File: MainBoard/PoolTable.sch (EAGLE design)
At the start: 77 parts, among them IC1 LM317MBSTT3, IC2 LM317MBSTT3, IC3 LM317MBSTT3, IC5 MIC2026-1YM, IC7 AP2331W-7, J1 USB_A_SMT_FEMALE, J2 USB_A_SMT_FEMALE, J4 SD_CARD_SOCKET, Q1 DMG1012T-7, Q2 DMG1012T-7, Q3 DMG1012T-7, U1 TMP102, U2 TMP102, U3 TMP102, U4 TMP102, U5 LAN9512-JZX, U6 FSUSB42UMX

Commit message: Syncing work
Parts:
- added SJ2, SJ3, SJ4, SJ5, SJ6, SJ7, SJ8, SJ9: (no value), jumper:SJ
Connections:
- removed net CPU1_CD1_SCL: CAM0.20, CAM1.20
- removed net CPU1_CD1_SDA: CAM0.21, CAM1.21
- new net CPU1_CAM0_IO0: SJ9.1
- new net CPU1_CAM0_IO1: SJ8.1
- new net CPU1_CAM0_SCL: SJ7.1
- new net CPU1_CAM0_SDA: SJ6.1
- new net CPU1_CAM1_IO0: SJ5.1
- new net CPU1_CAM1_IO1: SJ4.1
- new net CPU1_CAM1_SCL: SJ3.1
- new net CPU1_CAM1_SDA: SJ2.1
- net CPU1_CAM0_C_N: now also CPU1.144/CAM0_CN*
- net CPU1_CAM0_C_P: now also CPU1.142/CAM0_CP*
- net CPU1_CAM0_D0_N: now also CPU1.138/CAM0_DN0*
- net CPU1_CAM0_D0_P: now also CPU1.136/CAM0_DP0*
- net CPU1_CAM0_D1_N: now also CPU1.150/CAM0_DN1*
- net CPU1_CAM0_D1_P: now also CPU1.148/CAM0_DP1*
- net CPU1_GPIO28: now also SJ6.2
- net CPU1_GPIO29: now also SJ7.2
- net CPU1_GPIO30: now also SJ8.2
- net CPU1_GPIO31: now also SJ9.2
- net CPU1_SCL0: now also SJ3.2
- net CPU1_SCL1: now also SJ5.2
- net CPU1_SDA0: now also SJ2.2
- net CPU1_SDA1: now also SJ4.2
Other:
- note added: "I2C MAY BE CONFIGURED WRONG TO HAVE ACCESS TO BOTH BUSSES"

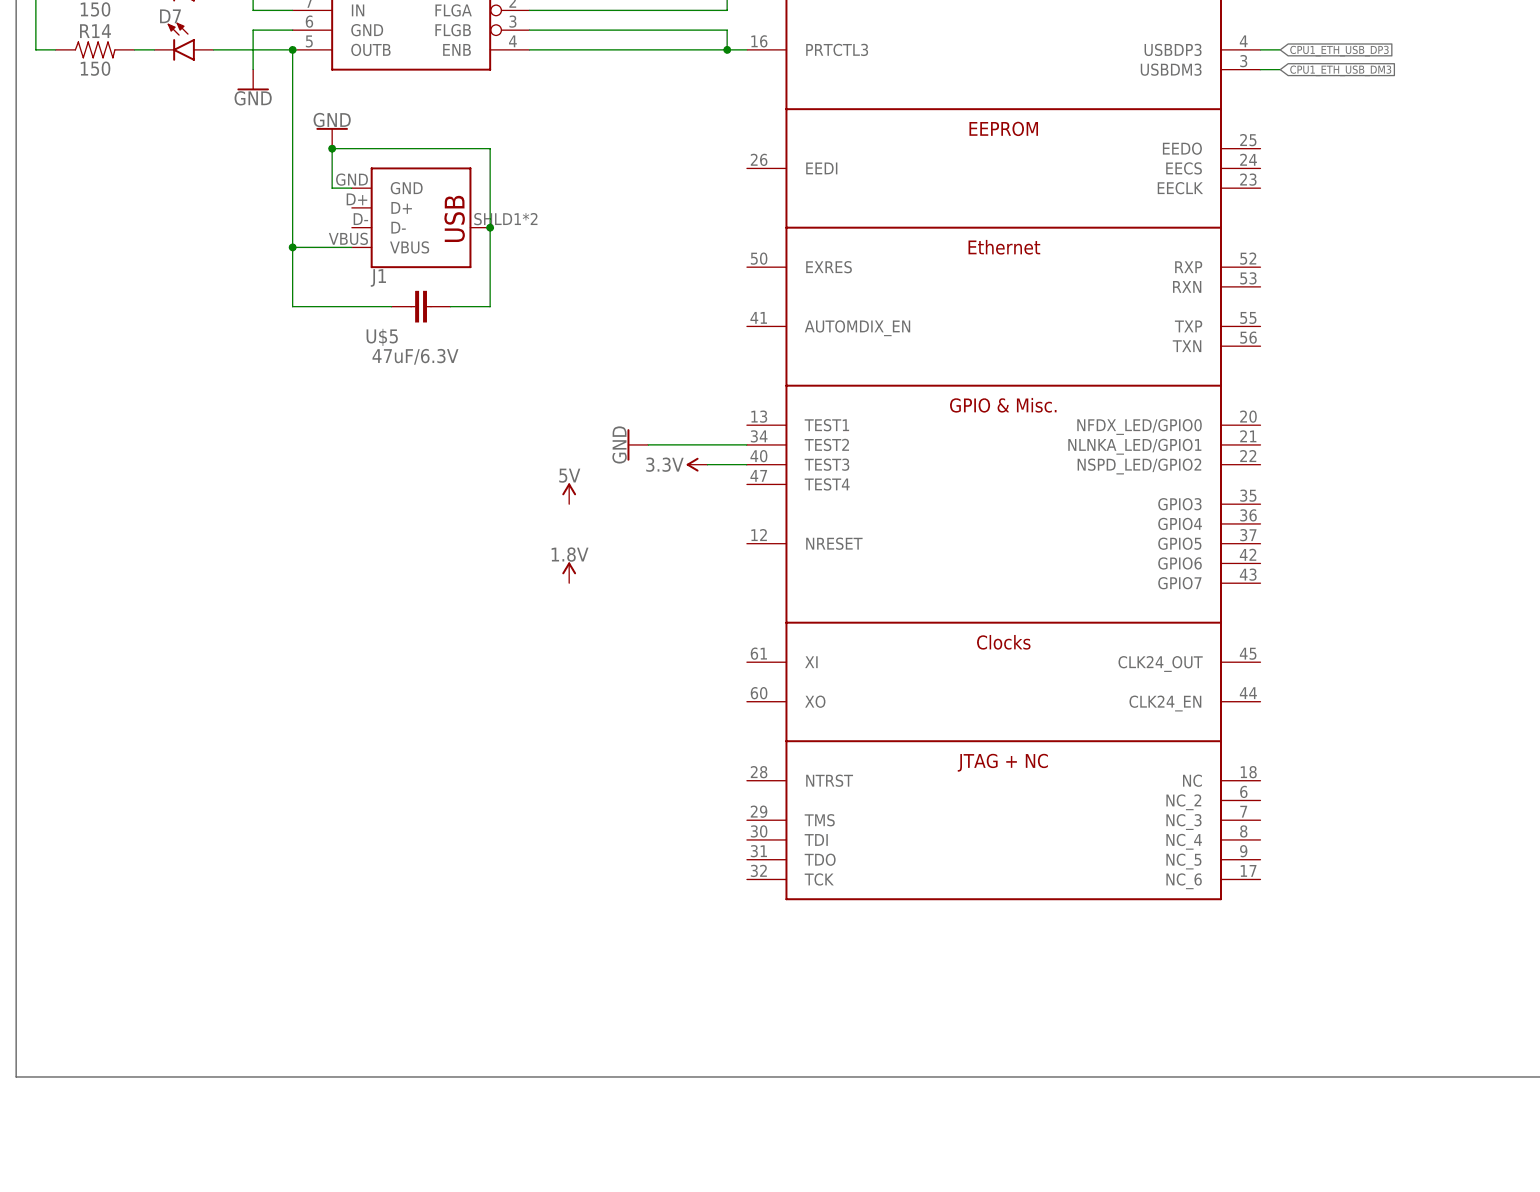
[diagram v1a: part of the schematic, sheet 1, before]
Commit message: Added EEPROM for LAN9512
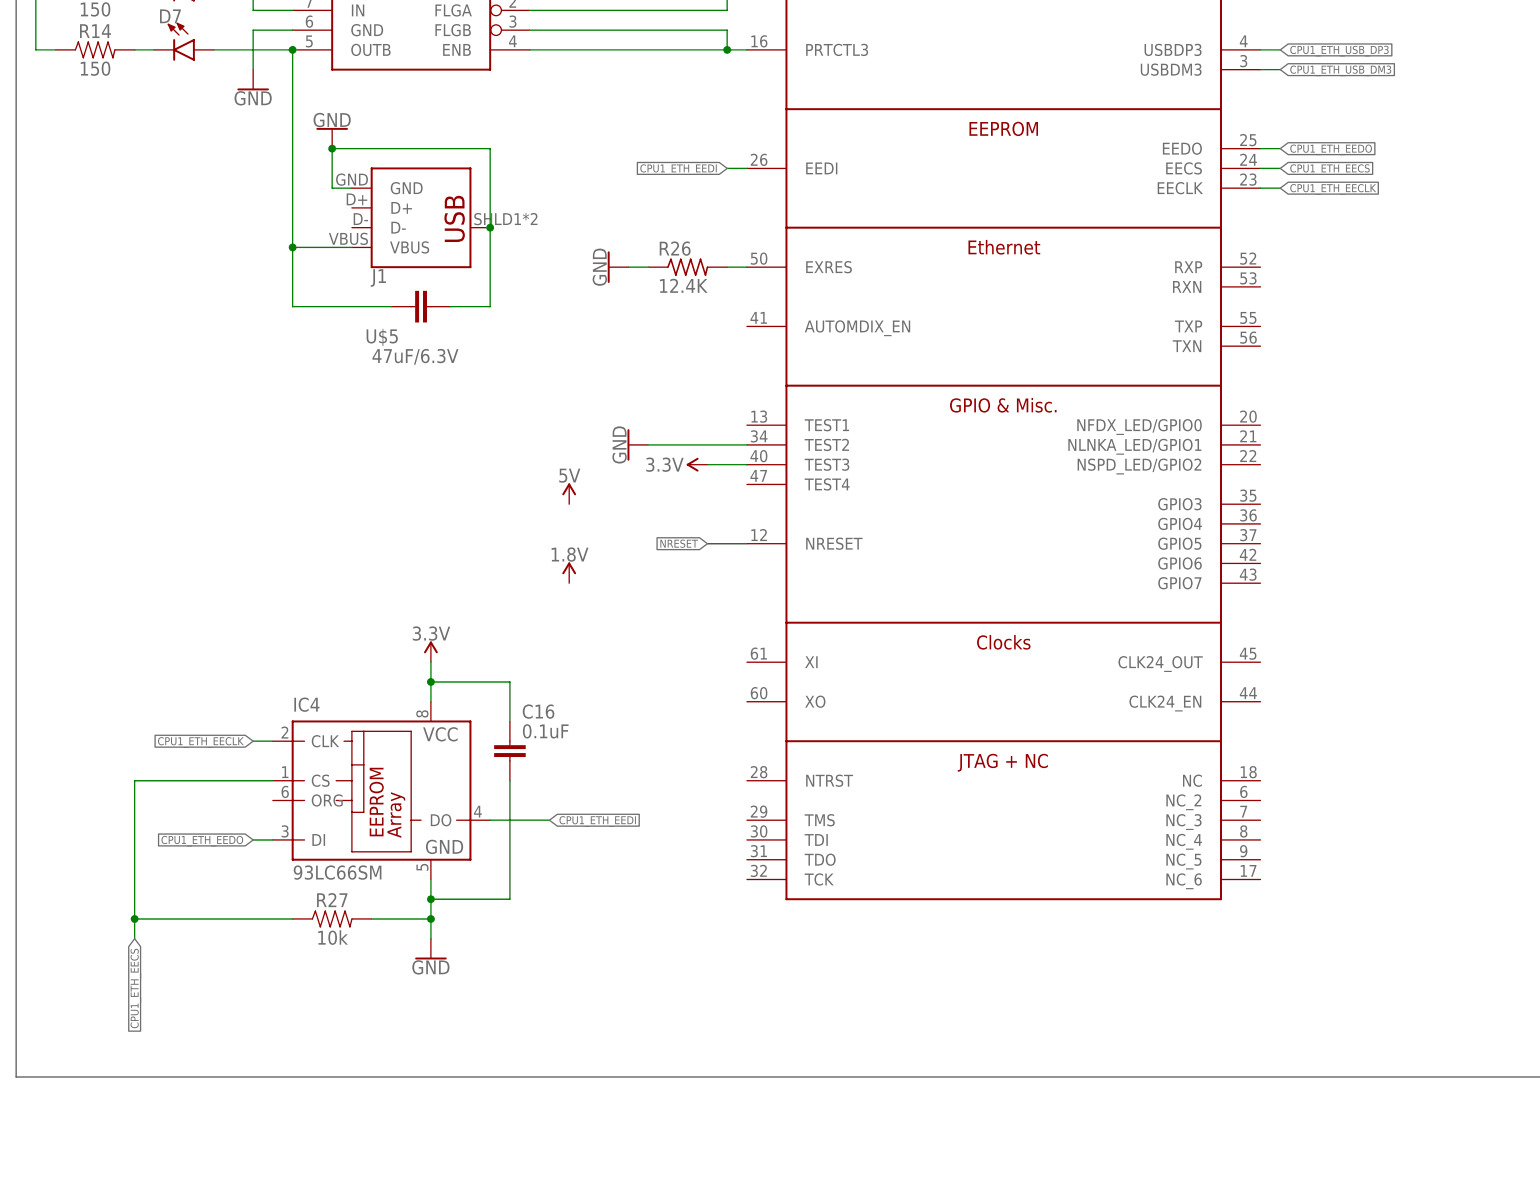
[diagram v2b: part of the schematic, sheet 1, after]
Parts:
- added C16: 0.1uF, SparkFun-Capacitors:0.1UF-0402-16V-10%
- added IC4: 93LC66SM, microchip:93LC66SM
- added R26: 12.4K, adafruit:R-US_R0603
- added R27: 10k, SparkFun-Resistors:10KOHM-0603-1/10W-1%
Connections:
- new net CPU1_ETH_EECLK: IC4.CLK, U5.EECLK
- new net CPU1_ETH_EECS: IC4.CS, R27.1, U5.EECS
- new net CPU1_ETH_EEDI: IC4.DO, U5.EEDI
- new net CPU1_ETH_EEDO: IC4.DI, U5.EEDO
- new net N$4: R26.2, U5.EXRES
- new net NRESET: U5.NRESET
- net 3.3V: now also C16.1, IC4.VCC
- net GND: now also C16.2, IC4.GND, R26.1, R27.2
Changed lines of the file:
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@@
 <?xml version="1.0" encoding="utf-8"?>
 <!DOCTYPE eagle SYSTEM "eagle.dtd">
-<eagle version="9.3.0">
+<eagle version="9.2.2">
 <drawing>
 <settings>
@@
 <part name="SJ8" library="jumper" library_urn="urn:adsk.eagle:library:252" deviceset="SJ" device="" package3d_urn="urn:adsk.eagle:package:15471/1"/>
 <part name="SJ9" library="jumper" library_urn="urn:adsk.eagle:library:252" deviceset="SJ" device="" package3d_urn="urn:adsk.eagle:package:15471/1"/>
+<part name="R26" library="adafruit" deviceset="R-US_" device="R0603" value="12.4K"/>
+<part name="GND23" library="SparkFun-PowerSymbols" deviceset="GND" device=""/>
+<part name="IC4" library="microchip" library_urn="urn:adsk.eagle:library:294" deviceset="93*" device="SM" package3d_urn="urn:adsk.eagle:package:20798/1" technology="LC66"/>
+<part name="R27" library="SparkFun-Resistors" deviceset="10KOHM" device="-0603-1/10W-1%" value="10k"/>
+<part name="GND24" library="SparkFun-PowerSymbols" deviceset="GND" device=""/>
+<part name="C16" library="SparkFun-Capacitors" deviceset="0.1UF" device="-0402-16V-10%" value="0.1uF"/>
+<part name="SUPPLY51" library="SparkFun-PowerSymbols" deviceset="3.3V" device=""/>
 </parts>
 <sheets>
@@
 <attribute name="NAME" x="309.88" y="104.14" size="1.778" layer="95" rot="R180"/>
 <attribute name="VALUE" x="309.88" y="110.49" size="1.778" layer="96" rot="R180"/>
+</instance>
+<instance part="R26" gate="G$1" x="96.52" y="314.96" smashed="yes">
+<attribute name="NAME" x="92.71" y="316.4586" size="1.778" layer="95"/>
+<attribute name="VALUE" x="92.71" y="311.658" size="1.778" layer="96"/>
+</instance>
+<instance part="GND23" gate="1" x="86.36" y="314.96" smashed="yes" rot="R270">
+<attribute name="VALUE" x="86.106" y="314.96" size="1.778" layer="96" rot="R270" align="top-center"/>
+</instance>
+<instance part="IC4" gate="G$1" x="55.88" y="246.38" smashed="yes">
+<attribute name="NAME" x="45.72" y="257.81" size="1.778" layer="95"/>
+<attribute name="VALUE" x="45.72" y="236.22" size="1.778" layer="96"/>
+</instance>
+<instance part="R27" gate="G$1" x="50.8" y="231.14" smashed="yes">
+<attribute name="NAME" x="50.8" y="232.664" size="1.778" layer="95" font="vector" align="bottom-center"/>
+<attribute name="VALUE" x="50.8" y="229.616" size="1.778" layer="96" font="vector" align="top-center"/>
+</instance>
+<instance part="GND24" gate="1" x="63.5" y="226.06" smashed="yes">
+<attribute name="VALUE" x="63.5" y="225.806" size="1.778" layer="96" align="top-center"/>
+</instance>
+<instance part="C16" gate="G$1" x="73.66" y="251.46" smashed="yes">
+<attribute name="NAME" x="75.184" y="256.921" size="1.778" layer="95" font="vector"/>
+<attribute name="VALUE" x="75.184" y="254.381" size="1.778" layer="96" font="vector"/>
+</instance>
+<instance part="SUPPLY51" gate="G$1" x="63.5" y="264.16" smashed="yes">
+<attribute name="VALUE" x="63.5" y="266.954" size="1.778" layer="96" align="bottom-center"/>
 </instance>
 </instances>
@@
 <pinref part="GND22" gate="1" pin="GND"/>
 </segment>
+<segment>
+<pinref part="R26" gate="G$1" pin="1"/>
+<pinref part="GND23" gate="1" pin="GND"/>
+<wire x1="91.44" y1="314.96" x2="88.9" y2="314.96" width="0.1524" layer="91"/>
+</segment>
+<segment>
+<pinref part="GND24" gate="1" pin="GND"/>
+<pinref part="IC4" gate="G$1" pin="GND"/>
+<wire x1="63.5" y1="228.6" x2="63.5" y2="231.14" width="0.1524" layer="91"/>
+<pinref part="R27" gate="G$1" pin="2"/>
+<wire x1="63.5" y1="231.14" x2="63.5" y2="233.68" width="0.1524" layer="91"/>
+<wire x1="63.5" y1="233.68" x2="63.5" y2="236.22" width="0.1524" layer="91"/>
+<wire x1="55.88" y1="231.14" x2="63.5" y2="231.14" width="0.1524" layer="91"/>
+<junction x="63.5" y="231.14"/>
+<pinref part="C16" gate="G$1" pin="2"/>
+<wire x1="73.66" y1="248.92" x2="73.66" y2="233.68" width="0.1524" layer="91"/>
+<wire x1="73.66" y1="233.68" x2="63.5" y2="233.68" width="0.1524" layer="91"/>
+<junction x="63.5" y="233.68"/>
+</segment>
 </net>
 <net name="CPU1_SDA0" class="0">
@@
 <pinref part="SUPPLY50" gate="G$1" pin="3.3V"/>
 <wire x1="264.16" y1="111.76" x2="256.54" y2="111.76" width="0.1524" layer="91"/>
+</segment>
+<segment>
+<pinref part="IC4" gate="G$1" pin="VCC"/>
+<wire x1="63.5" y1="259.08" x2="63.5" y2="261.62" width="0.1524" layer="91"/>
+<pinref part="C16" gate="G$1" pin="1"/>
+<wire x1="63.5" y1="261.62" x2="63.5" y2="264.16" width="0.1524" layer="91"/>
+<wire x1="63.5" y1="261.62" x2="73.66" y2="261.62" width="0.1524" layer="91"/>
+<wire x1="73.66" y1="261.62" x2="73.66" y2="256.54" width="0.1524" layer="91"/>
+<junction x="63.5" y="261.62"/>
+<pinref part="SUPPLY51" gate="G$1" pin="3.3V"/>
 </segment>
 </net>
@@
 </segment>
 </net>
+<net name="NRESET" class="0">
+<segment>
+<pinref part="U5" gate="A" pin="NRESET"/>
+<wire x1="99.06" y1="279.4" x2="104.14" y2="279.4" width="0.1524" layer="91"/>
+<label x="99.06" y="279.4" size="1.016" layer="95" rot="R180" xref="yes"/>
+</segment>
+</net>
+<net name="N$4" class="0">
+<segment>
+<pinref part="U5" gate="A" pin="EXRES"/>
+<pinref part="R26" gate="G$1" pin="2"/>
+<wire x1="104.14" y1="314.96" x2="101.6" y2="314.96" width="0.1524" layer="91"/>
+</segment>
+</net>
+<net name="CPU1_ETH_EEDO" class="0">
+<segment>
+<pinref part="U5" gate="A" pin="EEDO"/>
+<wire x1="172.72" y1="330.2" x2="170.18" y2="330.2" width="0.1524" layer="91"/>
+<label x="172.72" y="330.2" size="1.016" layer="95" xref="yes"/>
+</segment>
+<segment>
+<pinref part="IC4" gate="G$1" pin="DI"/>
+<wire x1="40.64" y1="241.3" x2="43.18" y2="241.3" width="0.1524" layer="91"/>
+<label x="40.64" y="241.3" size="1.016" layer="95" rot="R180" xref="yes"/>
+</segment>
+</net>
+<net name="CPU1_ETH_EECS" class="0">
+<segment>
+<pinref part="U5" gate="A" pin="EECS"/>
+<wire x1="172.72" y1="327.66" x2="170.18" y2="327.66" width="0.1524" layer="91"/>
+<label x="172.72" y="327.66" size="1.016" layer="95" xref="yes"/>
+</segment>
+<segment>
+<pinref part="IC4" gate="G$1" pin="CS"/>
+<wire x1="25.4" y1="228.6" x2="25.4" y2="231.14" width="0.1524" layer="91"/>
+<wire x1="25.4" y1="231.14" x2="25.4" y2="248.92" width="0.1524" layer="91"/>
+<wire x1="25.4" y1="248.92" x2="43.18" y2="248.92" width="0.1524" layer="91"/>
+<label x="25.4" y="228.6" size="1.016" layer="95" rot="R270" xref="yes"/>
+<pinref part="R27" gate="G$1" pin="1"/>
+<wire x1="45.72" y1="231.14" x2="25.4" y2="231.14" width="0.1524" layer="91"/>
+<junction x="25.4" y="231.14"/>
+</segment>
+</net>
+<net name="CPU1_ETH_EECLK" class="0">
+<segment>
+<pinref part="U5" gate="A" pin="EECLK"/>
+<wire x1="172.72" y1="325.12" x2="170.18" y2="325.12" width="0.1524" layer="91"/>
+<label x="172.72" y="325.12" size="1.016" layer="95" xref="yes"/>
+</segment>
+<segment>
+<pinref part="IC4" gate="G$1" pin="CLK"/>
+<wire x1="40.64" y1="254" x2="43.18" y2="254" width="0.1524" layer="91"/>
+<label x="40.64" y="254" size="1.016" layer="95" rot="R180" xref="yes"/>
+</segment>
+</net>
+<net name="CPU1_ETH_EEDI" class="0">
+<segment>
+<pinref part="U5" gate="A" pin="EEDI"/>
+<wire x1="101.6" y1="327.66" x2="104.14" y2="327.66" width="0.1524" layer="91"/>
+<label x="101.6" y="327.66" size="1.016" layer="95" rot="R180" xref="yes"/>
+</segment>
+<segment>
+<pinref part="IC4" gate="G$1" pin="DO"/>
+<wire x1="71.12" y1="243.84" x2="78.74" y2="243.84" width="0.1524" layer="91"/>
+<label x="78.74" y="243.84" size="1.016" layer="95" xref="yes"/>
+</segment>
+</net>

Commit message: Duplicated CM3 and mostly finished USB hub
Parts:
- added C17, C19, C20, C21, C22, C23, C24, C25, C26, C27, C28, C29, C30, C32, C33, C42, C44, C45, C46, C47, C48, C49, C50, C51, C52, C53, C54, C55, C57, C58: 0.1uF, SparkFun-Capacitors:1.0UF-0402-16V-10%
- added C18, C37, C43: 1.0uF, SparkFun-Capacitors:1.0UF-0402-16V-10%
- added C31, C34, C56, C59: 4.7uF, SparkFun-Capacitors:1.0UF-0402-16V-10%
- added C35, C36, C60, C61: 33pF, SparkFun-Capacitors:33PF-0603-50V-5%
- added C38, C41: 0.1uF, SparkFun-Capacitors:0.1UF-0402-16V-10%
- added C39, C40: 4.7uF, SparkFun-Capacitors:4.7UF-0603-6.3V-(10%)
- added CAM2, CAM3: 54548-2271, SamacSys_Parts:54548-2271
- added CPU2: RPI_COMPUTE, e14_Rpi_Compute_RevC:RPI_COMPUTE
- added D10, D10-FULLDUPLEX, D10-FULLDUPLEX1, D11, D11_LINK, D11_LINK1, D12: GREEN, SparkFun-LED:LED-GREEN0603
- added D12_FASTETHER, D12_FASTETHER1: Yellow, SparkFun-LED:LED-YELLOW0603
- added FB1, FB2, FB3, FB4: 0.05Ω/2A, SparkFun-Coils:FERRITE_BEAD-0603
- added IC6: MIC2026-1YM, micrel:MIC2026-1YM
- added IC8: 93LC66SM, microchip:93LC66SM
- added J5, J6: USB_A_SMT_FEMALE, SparkFun-Connectors:USB_A_SMT_FEMALE
- added J7: (no value), SparkFun-Connectors:USB_MICRO-B_SMT
- added J8: SD_CARD_SOCKET, SparkFun-Connectors:SD_CARD_SOCKET
- added JP2, JP3, JP4: (no value), adafruit:PINHD-1X3
- added Q4, Q5, Q6: DMG1012T-7, SamacSys_Parts:DMG1012T-7
- added R28, R50, R52: 12.4K, adafruit:R-US_R0603
- added R29, R53: 1M, SparkFun-Resistors:1MOHM-0603-1/4W-5%
- added R30, R54: 10K, adafruit:R-US_R0603
- added R31, R55: 12K, adafruit:R-US_R0603
- added R32, R33, R34, R56, R57, R58: 332R, adafruit:R-US_R0603
- added R35, R36, R37, R38: 4.7k, SparkFun-Resistors:4.7KOHM-0603-1/10W-1%
- added R39, R40, R44: 150, SparkFun-Resistors:150OHM-0603-1/10W-1%
- added R41, R42, R43: 47k, SparkFun-Resistors:47KOHM-0603-1/10W-1%
- added R45, R46, R47, R48, R49: 100K, SparkFun-Resistors:100KOHM-0402-1/16W-1%
- added R51: 10k, SparkFun-Resistors:10KOHM-0603-1/10W-1%
- added SJ10, SJ11, SJ12, SJ13, SJ14, SJ15, SJ16, SJ17, SJ18: (no value), jumper:SJ
- added U$6, U$7: 47uF/6.3V, SparkFun-Capacitors:47UF
- added U7: LAN9512-JZX, External:LAN9512-JZX
- added U8: FSUSB42UMX, FSUSB42UMX:FSUSB42UMX
- added Y1, Y2: 25MHz, SparkFun-Clocks:CRYSTAL-GROUNDEDSMD-3.2X2.5
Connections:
- removed net CPU1_CAM0_IO_0: CAM0.17
- removed net CPU1_CAM0_IO_1: CAM0.18
- removed net CPU1_CAM1_IO_0: CAM1.17
- removed net CPU1_CAM1_IO_1: CAM1.18
- removed net CPU1_SCL0: CPU1.5/GPIO1, R7.1, SJ3.2, U$1.SCL, U$2.SCL, U$3.SCL, U1.SCL, U2.SCL, U3.SCL, U4.ADD0, U4.SCL
- removed net CPU1_SDA0: CPU1.3/GPIO0, R8.1, SJ2.2, U$1.SDA, U$2.SDA, U$3.SDA, U1.SDA, U2.SDA, U3.ADD0, U3.SDA, U4.SDA
- new net CPU1_ETH_18ETHPLL: C17.2, FB1.1, U5.VDD18ETHPLL
- new net CPU1_ETH_18USBPLL: C18.2, FB1.2, U5.VDD18USBPLL
- new net CPU1_ETH_PWR1: D11.A, IC6.OUTA, J6.VBUS, U$6.1
- new net CPU1_ETH_PWR4: D10.A, IC6.OUTB, J5.VBUS, U$7.1
- new net CPU1_ETH_RXN: U5.RXN
- new net CPU1_ETH_RXP: U5.RXP
- new net CPU1_ETH_TXN: U5.TXN
- new net CPU1_ETH_TXP: U5.TXP
- new net CPU1_GPIO0: CPU1.3/GPIO0, R8.1, SJ2.2
- new net CPU1_GPIO1: CPU1.5/GPIO1, R7.1, SJ3.2
- new net CPU2_CAM0_C_N: CAM3.8, CPU2.144/CAM0_CN*
- new net CPU2_CAM0_C_P: CAM3.9, CPU2.142/CAM0_CP*
- new net CPU2_CAM0_D0_N: CAM3.2, CPU2.138/CAM0_DN0*
- new net CPU2_CAM0_D0_P: CAM3.3, CPU2.136/CAM0_DP0*
- new net CPU2_CAM0_D1_N: CAM3.5, CPU2.150/CAM0_DN1*
- new net CPU2_CAM0_D1_P: CAM3.6, CPU2.148/CAM0_DP1*
- new net CPU2_CAM0_IO0: CAM3.17, SJ18.1
- new net CPU2_CAM0_IO1: CAM3.18, SJ17.1
- new net CPU2_CAM0_SCL: SJ16.1
- new net CPU2_CAM0_SDA: SJ15.1
- new net CPU2_CAM1_C_N: CAM2.8, CPU2.149/CAM1_CN*
- new net CPU2_CAM1_C_P: CAM2.9, CPU2.147/CAM1_CP*
- new net CPU2_CAM1_D0_N: CAM2.2, CPU2.161/CAM1_DN0*
- new net CPU2_CAM1_D0_P: CAM2.3, CPU2.159/CAM1_DP0*
- new net CPU2_CAM1_D1_N: CAM2.5, CPU2.155/CAM1_DN1*
- new net CPU2_CAM1_D1_P: CAM2.6, CPU2.153/CAM1_DP1*
- new net CPU2_CAM1_D2_N: CAM2.11, CPU2.143/CAM1_DN2*
- new net CPU2_CAM1_D2_P: CAM2.12, CPU2.141/CAM1_DP2*
- new net CPU2_CAM1_D3_N: CAM2.14, CPU2.137/CAM1_DN3*
- new net CPU2_CAM1_D3_P: CAM2.15, CPU2.135/CAM1_DP3*
- new net CPU2_CAM1_IO0: CAM2.17, SJ14.1
- new net CPU2_CAM1_IO1: CAM2.18, SJ13.1
- new net CPU2_CAM1_SCL: SJ12.1
- new net CPU2_CAM1_SDA: SJ11.1
- new net CPU2_EMMC_DISABLE_N: CPU2.2/EMMC_DISABLE_N, Q5.D
- new net CPU2_EMMC_EN_N_1V8: CPU2.90/GPIO47_1V8, Q6.G, R45.2
- new net CPU2_ETH_18ETHPLL: C42.2, FB3.1, U7.VDD18ETHPLL
- new net CPU2_ETH_18USBPLL: C43.2, FB3.2, U7.VDD18USBPLL
- new net CPU2_ETH_EECLK: IC8.CLK, U7.EECLK
- new net CPU2_ETH_EECS: IC8.CS, R51.1, U7.EECS
- new net CPU2_ETH_EEDI: IC8.DO, U7.EEDI
- new net CPU2_ETH_EEDO: IC8.DI, U7.EEDO
- new net CPU2_ETH_RXN: U7.RXN
- new net CPU2_ETH_RXP: U7.RXP
- new net CPU2_ETH_TXN: U7.TXN
- new net CPU2_ETH_TXP: U7.TXP
- new net CPU2_ETH_USBDM: U7.USBDM0, U8.HSD1-
- new net CPU2_ETH_USBDP: U7.USBDP0, U8.HSD1+
- new net CPU2_ETH_USB_DM2: J6.D-, U7.USBDM2
- new net CPU2_ETH_USB_DM3: J5.D-, U7.USBDM3
- new net CPU2_ETH_USB_DP2: J6.D+, U7.USBDP2
- new net CPU2_ETH_USB_DP3: J5.D+, U7.USBDP3
- new net CPU2_ETH_VDD18CORE: C57.2, C58.2, C59.2, U7.VDD18CORE, U7.VDD18CORE_2
- new net CPU2_ETH_VDD3A: C44.2, C45.2, C46.2, C47.2, C48.2, C49.2, C50.2, FB4.2, U7.VDD33A_1, U7.VDD33A_2, U7.VDD33A_3, U7.VDD33A_4, U7.VDD33A_5, U7.VDD33A_6, U7.VDD33A_7
- new net CPU2_GPIO0: CPU2.3/GPIO0, R36.1, SJ11.2
- new net CPU2_GPIO1: CPU2.5/GPIO1, R35.1, SJ12.2
- new net CPU2_GPIO12: CPU2.45/GPIO12
- new net CPU2_GPIO13: CPU2.47/GPIO13
- new net CPU2_GPIO14: CPU2.51/GPIO14
- new net CPU2_GPIO15: CPU2.53/GPIO15
- new net CPU2_GPIO16: CPU2.57/GPIO16
- new net CPU2_GPIO17: CPU2.59/GPIO17
- new net CPU2_GPIO18: CPU2.63/GPIO18
- new net CPU2_GPIO22: CPU2.75/GPIO22
- new net CPU2_GPIO23: CPU2.77/GPIO23
- new net CPU2_GPIO24: CPU2.81/GPIO24
- new net CPU2_GPIO25: CPU2.83/GPIO25
- new net CPU2_GPIO26: CPU2.87/GPIO26
- new net CPU2_GPIO27: CPU2.89/GPIO27
- new net CPU2_GPIO28: CPU2.28/GPIO28, R46.1, SJ15.2
- new net CPU2_GPIO29: CPU2.30/GPIO29, R47.1, SJ16.2
- new net CPU2_GPIO30: CPU2.34/GPIO30, SJ17.2
- new net CPU2_GPIO31: CPU2.36/GPIO31, SJ18.2
- new net CPU2_GPIO32: CPU2.46/GPIO32
- new net CPU2_GPIO33: CPU2.48/GPIO33
- new net CPU2_GPIO34: CPU2.52/GPIO34
- new net CPU2_GPIO35: CPU2.54/GPIO35
- new net CPU2_GPIO36: CPU2.58/GPIO36
- new net CPU2_GPIO37: CPU2.60/GPIO37
- new net CPU2_GPIO38: CPU2.64/GPIO38
- new net CPU2_GPIO39: CPU2.66/GPIO39
- new net CPU2_GPIO4: CPU2.15/GPIO4, SJ13.2
- new net CPU2_GPIO40: CPU2.70/GPIO40
- new net CPU2_GPIO41: CPU2.72/GPIO41
- new net CPU2_GPIO42: CPU2.76/GPIO42
- new net CPU2_GPIO43: CPU2.78/GPIO43
- new net CPU2_GPIO44: CPU2.82/GPIO44, R48.1
- new net CPU2_GPIO45: CPU2.84/GPIO45, R49.1
- new net CPU2_GPIO5: CPU2.17/GPIO5, SJ14.2
- new net CPU2_GPIO6: CPU2.21/GPIO6
- new net CPU2_GPIO7: CPU2.23/GPIO7
- new net CPU2_GPIO8: CPU2.27/GPIO8
- new net CPU2_SCL1: CPU2.11/GPIO3, R37.1
- new net CPU2_SDA1: CPU2.9/GPIO2, R38.1
- new net CPU2_SD_CLK: CPU2.10/NC, J8.CLK
- new net CPU2_SD_CMD: CPU2.12/NC, J8.CMD
- new net CPU2_SD_D0: CPU2.16/NC, J8.DAT0
- new net CPU2_SD_D1: CPU2.18/NC, J8.DAT1
- new net CPU2_SD_D2: CPU2.22/NC, J8.DAT2
- new net CPU2_SD_D3: CPU2.24/NC, J8.CD/DAT3
- new net CPU2_SD_VREF: C40.2, CPU2.4/NC, CPU2.6/NC, SJ10.1
- new net CPU2_SPI0_MISO: CPU2.29/GPIO9
- new net CPU2_SPI0_MOSI: CPU2.33/GPIO10
- new net CPU2_SPI0_SCLK: CPU2.35/GPIO11
- new net CPU2_SPI1_MISO: CPU2.65/GPIO19
- new net CPU2_SPI1_MOSI: CPU2.69/GPIO20
- new net CPU2_SPI1_SCLK: CPU2.71/GPIO21
- new net CPU2_USB_D_N: CPU2.167/USB_DM**, U8.D-
- new net CPU2_USB_D_P: CPU2.165/USB_DP**, U8.D+
- new net CPU2_VBUSB: J7.VBUS, JP3.1, Q4.G, R41.2
- new net N$13: R30.2, U5.AUTOMDIX_EN
- new net N$14: JP2.2, R30.1
- new net N$24: R31.2, U5.USBRBIAS
- new net N$25: D12_FASTETHER.C, R33.2
- new net N$26: D10-FULLDUPLEX.C, R32.2
- new net N$27: D11_LINK.C, R34.2
- new net N$28: R32.1, U5.NFDX_LED/GPIO0
- new net N$29: R34.1, U5.NLNKA_LED/GPIO1
- new net N$30: R33.1, U5.NSPD_LED/GPIO2
- new net N$31: IC6.ENA, IC6.FLGA, U7.PRTXTL2
- new net N$32: IC6.ENB, IC6.FLGB, U7.PRTCTL3
- new net N$33: D11.C, R39.2
- new net N$34: D10.C, R40.2
- new net N$35: Q4.S, R42.1, U8.SEL
- new net N$36: J7.D+, U8.HSD2+
- new net N$37: J7.D-, U8.HSD2-
- new net N$38: JP3.2, Q5.G, R43.2
- new net N$39: D12.C, Q5.S, Q6.D
- new net N$40: D12.A, R44.1
- new net N$41: R50.2, U7.EXRES
- new net N$42: R52.2, U7.VBUS_DET
- new net N$43: C60.1, R53.1, U7.XI, Y1.1
- new net N$44: C61.1, R53.2, U7.XO, Y1.2
- new net N$45: R54.2, U7.AUTOMDIX_EN
- new net N$46: JP4.2, R54.1
- new net N$47: R55.2, U7.USBRBIAS
- new net N$48: D10-FULLDUPLEX1.C, R56.2
- new net N$49: D12_FASTETHER1.C, R57.2
- new net N$5: R28.2, U5.VBUS_DET
- new net N$50: D11_LINK1.C, R58.2
- new net N$51: R56.1, U7.NFDX_LED/GPIO0
- new net N$52: R58.1, U7.NLNKA_LED/GPIO1
- new net N$53: R57.1, U7.NSPD_LED/GPIO2
- new net N$7: C35.1, R29.1, U5.XI, Y2.1
- new net N$8: C36.1, R29.2, U5.XO, Y2.2
- net 1.8V: now also CPU2.183/1V8, CPU2.184/1V8, CPU2.185/1V8, CPU2.186/1V8, R45.1
- net 3.3V: now also C26.2, C27.2, C28.2, C29.2, C30.2, C31.2, C38.2, C39.1, C41.1, C51.2, C52.2, C53.2, C54.2, C55.2, C56.2, CAM2.22, CAM3.22, CPU2.189/VDAC, CPU2.190/VDAC, CPU2.191/3V3, CPU2.192/3V3, CPU2.193/3V3, CPU2.194/3V3, CPU2.39/GPIO0-27_VREF, CPU2.40/GPIO0-27_VREF, CPU2.41/GPIO28-45_VREF, CPU2.42/GPIO28-45_VREF, D10-FULLDUPLEX.A, D10-FULLDUPLEX1.A, D11_LINK.A, D11_LINK1.A, D12_FASTETHER.A, D12_FASTETHER1.A, FB2.1, FB4.1, IC8.VCC, J8.VDD, JP2.1, JP4.1, R28.1, R42.2, R44.2, R52.1, SJ10.2, U7.TEST3, U7.VDD33IO_1, U7.VDD33IO_2, U7.VDD33IO_3, U7.VDD33IO_4, U7.VDD33IO_5, U8.VCC
- net 5V: now also C37.2, CPU2.197/VBAT, CPU2.198/VBAT, CPU2.199/VBAT, CPU2.200/VBAT, IC6.IN, R35.2, R36.2, R37.2, R38.2
- net CPU1_CAM0_IO0: now also CAM0.17
- net CPU1_CAM0_IO1: now also CAM0.18
- net CPU1_CAM1_IO0: now also CAM1.17
- net CPU1_CAM1_IO1: now also CAM1.18
- net CPU1_ETH_USB_DM2: now also J2.D-
- net CPU1_ETH_USB_DM3: now also J1.D-
- net CPU1_ETH_USB_DP2: now also J2.D+
- net CPU1_ETH_USB_DP3: now also J1.D+
- net CPU1_ETH_VDD18CORE: now also C32.2, C33.2, C34.2
- net CPU1_ETH_VDD3A: now also C19.2, C20.2, C21.2, C22.2, C23.2, C24.2, C25.2, FB2.2
- net CPU1_GPIO4: now also SJ4.2
- net CPU1_GPIO5: now also SJ5.2
- net CPU1_SCL1: now also U$1.SCL, U$2.SCL, U$3.SCL, U1.SCL, U2.SCL, U3.SCL, U4.ADD0, U4.SCL; no longer SJ5.2
- net CPU1_SDA1: now also U$1.SDA, U$2.SDA, U$3.SDA, U1.SDA, U2.SDA, U3.ADD0, U3.SDA, U4.SDA; no longer SJ4.2
- net GND: now also C17.1, C18.1, C19.1, C20.1, C21.1, C22.1, C23.1, C24.1, C25.1, C26.1, C27.1, C28.1, C29.1, C30.1, C31.1, C32.1, C33.1, C34.1, C35.2, C36.2, C37.1, C38.1, C39.2, C40.1, C41.2, C42.1, C43.1, C44.1, C45.1, C46.1, C47.1, C48.1, C49.1, C50.1, C51.1, C52.1, C53.1, C54.1, C55.1, C56.1, C57.1, C58.1, C59.1, C60.2, C61.2, CAM2.1, CAM2.10, CAM2.13, CAM2.16, CAM2.19, CAM2.23, CAM2.24, CAM2.4, CAM2.7, CAM3.1, CAM3.10, CAM3.13, CAM3.16, CAM3.19, CAM3.23, CAM3.24, CAM3.4, CAM3.7, CPU2.1/GND, CPU2.103/GND, CPU2.104/GND, CPU2.109/GND, CPU2.110/GND, CPU2.115/GND, CPU2.116/GND, CPU2.121/GND, CPU2.122/GND, CPU2.127/GND, CPU2.13/GND, CPU2.133/GND, CPU2.134/GND, CPU2.139/GND, CPU2.14/NC, CPU2.140/GND, CPU2.145/GND, CPU2.146/GND, CPU2.151/GND, CPU2.152/GND, CPU2.157/GND, CPU2.163/GND, CPU2.164/GND, CPU2.169/GND, CPU2.170/GND, CPU2.181/GND, CPU2.182/GND, CPU2.187/GND, CPU2.188/GND, CPU2.19/GND, CPU2.195/GND, CPU2.196/GND, CPU2.20/NC, CPU2.25/GND, CPU2.26/GND, CPU2.31/GND, CPU2.32/GND, CPU2.37/GND, CPU2.38/GND, CPU2.43/GND, CPU2.44/GND, CPU2.49/GND, CPU2.50/GND, CPU2.55/GND, CPU2.56/GND, CPU2.61/GND, CPU2.62/GND, CPU2.67/GND, CPU2.68/GND, CPU2.7/GND, CPU2.73/GND, CPU2.74/GND, CPU2.79/GND, CPU2.8/NC, CPU2.80/GND, CPU2.85/GND, CPU2.86/GND, CPU2.91/GND, CPU2.92/GND, CPU2.97/GND, CPU2.98/GND, IC6.GND, IC8.GND, J5.GND, J5.SHIELD, J6.GND, J6.SHIELD, J7.GND, J7.SHIELD, J8.SH@1, J8.SH@2, J8.VSS1, J8.VSS2, JP2.3, JP3.3, JP4.3, Q4.D, Q6.S, R31.1, R39.1, R40.1, R41.1, R43.1, R46.2, R47.2, R48.2, R49.2, R50.1, R51.2, R55.1, U$6.2, U$7.2, U7.EPAD, U7.TEST2, U8.GND, Y1.3, Y2.3
- net NRESET: now also U7.NRESET
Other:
- note added: "A"
- note added: "Board Wide Power Supplies Network Switching"
- note added: "CPU1 And Associated Components"
- note added: "CPU2 And Associated Components"
- note added: "Camera Connectors"
- note added: "EEPROM"
- note added: "Misc Components"
- note added: "Power Filtering"
- note removed: "I2C MAY BE CONFIGURED WRONG TO HAVE ACCESS TO BOTH BUSSES"
